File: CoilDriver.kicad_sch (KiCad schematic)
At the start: 25 parts, among them Q12 IRLML2803, Q13 SIRA99DP-T1-GE3, U3 DRV8235RTER

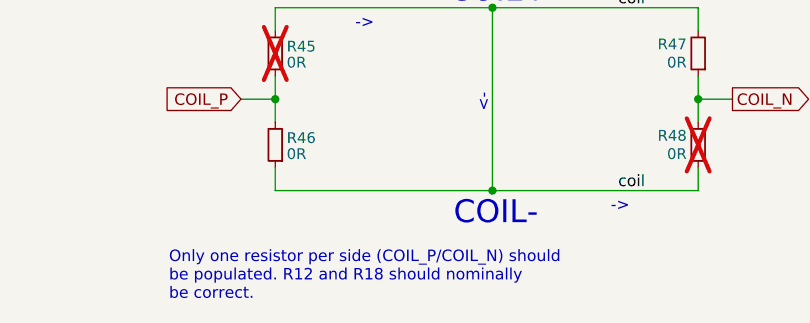
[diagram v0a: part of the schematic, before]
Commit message: Coil direction comment clarification
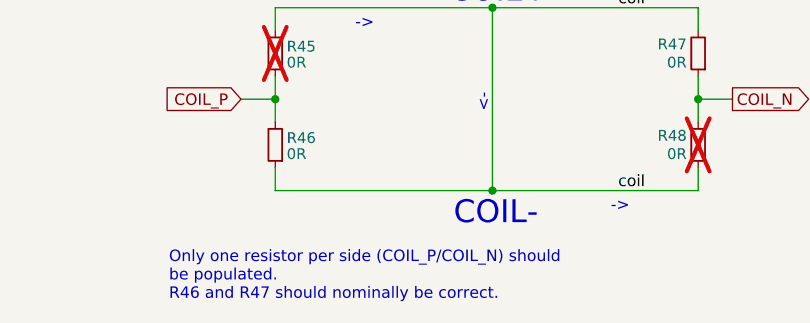
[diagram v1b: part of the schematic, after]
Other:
- note added: "Only one resistor per side (COIL_P/COIL_N) should be populated. R46 and R47 should nominally be correct."
- note removed: "Only one resistor per side (COIL_P/COIL_N) should be populated. R12 and R18 should nominally be correct."
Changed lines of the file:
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@@
 		)
 	)
-	(text "Only one resistor per side (COIL_P/COIL_N) should \nbe populated. R12 and R18 should nominally \nbe correct."
+	(text "Only one resistor per side (COIL_P/COIL_N) should \nbe populated. \nR46 and R47 should nominally be correct."
 		(exclude_from_sim no)
 		(at 42.799 168.529 0)
@@
 		)
 		(instances
-			(project "Z-"
+			(project "-Z"
 				(path "/446ceff1-46b8-4829-b15a-92d0d6c980a6/a90023fb-0fab-4c1a-9223-dcb77ef77cb2"
 					(reference "R37")
@@
 		)
 		(instances
-			(project "Z-"
+			(project "-Z"
 				(path "/446ceff1-46b8-4829-b15a-92d0d6c980a6/a90023fb-0fab-4c1a-9223-dcb77ef77cb2"
 					(reference "#PWR046")
@@
 		)
 		(instances
-			(project "Z-"
+			(project "-Z"
 				(path "/446ceff1-46b8-4829-b15a-92d0d6c980a6/a90023fb-0fab-4c1a-9223-dcb77ef77cb2"
 					(reference "R50")
@@
 		)
 		(instances
-			(project "Z-"
+			(project "-Z"
 				(path "/446ceff1-46b8-4829-b15a-92d0d6c980a6/a90023fb-0fab-4c1a-9223-dcb77ef77cb2"
 					(reference "R49")
@@
 		)
 		(instances
-			(project "Z-"
+			(project "-Z"
 				(path "/446ceff1-46b8-4829-b15a-92d0d6c980a6/a90023fb-0fab-4c1a-9223-dcb77ef77cb2"
 					(reference "R46")
@@
 		)
 		(instances
-			(project "Z-"
+			(project "-Z"
 				(path "/446ceff1-46b8-4829-b15a-92d0d6c980a6/a90023fb-0fab-4c1a-9223-dcb77ef77cb2"
 					(reference "#GND01")
@@
 		)
 		(instances
-			(project "Z-"
+			(project "-Z"
 				(path "/446ceff1-46b8-4829-b15a-92d0d6c980a6/a90023fb-0fab-4c1a-9223-dcb77ef77cb2"
 					(reference "#PWR043")
@@
 		)
 		(instances
-			(project "Z-"
+			(project "-Z"
 				(path "/446ceff1-46b8-4829-b15a-92d0d6c980a6/a90023fb-0fab-4c1a-9223-dcb77ef77cb2"
 					(reference "C9")
@@
 		)
 		(instances
-			(project "Z-"
+			(project "-Z"
 				(path "/446ceff1-46b8-4829-b15a-92d0d6c980a6/a90023fb-0fab-4c1a-9223-dcb77ef77cb2"
 					(reference "R42")
@@
 		)
 		(instances
-			(project "Z-"
+			(project "-Z"
 				(path "/446ceff1-46b8-4829-b15a-92d0d6c980a6/a90023fb-0fab-4c1a-9223-dcb77ef77cb2"
 					(reference "R43")
@@
 		)
 		(instances
-			(project "Z-"
+			(project "-Z"
 				(path "/446ceff1-46b8-4829-b15a-92d0d6c980a6/a90023fb-0fab-4c1a-9223-dcb77ef77cb2"
 					(reference "#PWR036")
@@
 		)
 		(instances
-			(project "Z-"
+			(project "-Z"
 				(path "/446ceff1-46b8-4829-b15a-92d0d6c980a6/a90023fb-0fab-4c1a-9223-dcb77ef77cb2"
 					(reference "C4")
@@
 		)
 		(instances
-			(project "Z-"
+			(project "-Z"
 				(path "/446ceff1-46b8-4829-b15a-92d0d6c980a6/a90023fb-0fab-4c1a-9223-dcb77ef77cb2"
 					(reference "R39")
@@
 		)
 		(instances
-			(project "Z-"
+			(project "-Z"
 				(path "/446ceff1-46b8-4829-b15a-92d0d6c980a6/a90023fb-0fab-4c1a-9223-dcb77ef77cb2"
 					(reference "#PWR045")
@@
 		)
 		(instances
-			(project "Z-"
+			(project "-Z"
 				(path "/446ceff1-46b8-4829-b15a-92d0d6c980a6/a90023fb-0fab-4c1a-9223-dcb77ef77cb2"
 					(reference "R51")
@@
 		)
 		(instances
-			(project "Z-"
+			(project "-Z"
 				(path "/446ceff1-46b8-4829-b15a-92d0d6c980a6/a90023fb-0fab-4c1a-9223-dcb77ef77cb2"
 					(reference "#PWR044")
@@
 		)
 		(instances
-			(project "Z-"
+			(project "-Z"
 				(path "/446ceff1-46b8-4829-b15a-92d0d6c980a6/a90023fb-0fab-4c1a-9223-dcb77ef77cb2"
 					(reference "#PWR039")
@@
 		)
 		(instances
-			(project "Z-"
+			(project "-Z"
 				(path "/446ceff1-46b8-4829-b15a-92d0d6c980a6/a90023fb-0fab-4c1a-9223-dcb77ef77cb2"
 					(reference "#PWR040")
@@
 		)
 		(instances
-			(project "Z-"
+			(project "-Z"
 				(path "/446ceff1-46b8-4829-b15a-92d0d6c980a6/a90023fb-0fab-4c1a-9223-dcb77ef77cb2"
 					(reference "Q12")
@@
 		)
 		(instances
-			(project "Z-"
+			(project "-Z"
 				(path "/446ceff1-46b8-4829-b15a-92d0d6c980a6/a90023fb-0fab-4c1a-9223-dcb77ef77cb2"
 					(reference "U3")
@@
 		)
 		(instances
-			(project "Z-"
+			(project "-Z"
 				(path "/446ceff1-46b8-4829-b15a-92d0d6c980a6/a90023fb-0fab-4c1a-9223-dcb77ef77cb2"
 					(reference "#PWR035")
@@
 		)
 		(instances
-			(project "Z-"
+			(project "-Z"
 				(path "/446ceff1-46b8-4829-b15a-92d0d6c980a6/a90023fb-0fab-4c1a-9223-dcb77ef77cb2"
 					(reference "C8")
@@
 		)
 		(instances
-			(project "Z-"
+			(project "-Z"
 				(path "/446ceff1-46b8-4829-b15a-92d0d6c980a6/a90023fb-0fab-4c1a-9223-dcb77ef77cb2"
 					(reference "#PWR038")
@@
 		)
 		(instances
-			(project "Z-"
+			(project "-Z"
 				(path "/446ceff1-46b8-4829-b15a-92d0d6c980a6/a90023fb-0fab-4c1a-9223-dcb77ef77cb2"
 					(reference "R41")
@@
 		)
 		(instances
-			(project "Z-"
+			(project "-Z"
 				(path "/446ceff1-46b8-4829-b15a-92d0d6c980a6/a90023fb-0fab-4c1a-9223-dcb77ef77cb2"
 					(reference "R47")
@@
 		)
 		(instances
-			(project "Z-"
+			(project "-Z"
 				(path "/446ceff1-46b8-4829-b15a-92d0d6c980a6/a90023fb-0fab-4c1a-9223-dcb77ef77cb2"
 					(reference "#PWR049")
@@
 		)
 		(instances
-			(project "Z-"
+			(project "-Z"
 				(path "/446ceff1-46b8-4829-b15a-92d0d6c980a6/a90023fb-0fab-4c1a-9223-dcb77ef77cb2"
 					(reference "#GND02")
@@
 		)
 		(instances
-			(project "Z-"
+			(project "-Z"
 				(path "/446ceff1-46b8-4829-b15a-92d0d6c980a6/a90023fb-0fab-4c1a-9223-dcb77ef77cb2"
 					(reference "#PWR051")
@@
 		)
 		(instances
-			(project "Z-"
+			(project "-Z"
 				(path "/446ceff1-46b8-4829-b15a-92d0d6c980a6/a90023fb-0fab-4c1a-9223-dcb77ef77cb2"
 					(reference "C5")
@@
 		)
 		(instances
-			(project "Z-"
+			(project "-Z"
 				(path "/446ceff1-46b8-4829-b15a-92d0d6c980a6/a90023fb-0fab-4c1a-9223-dcb77ef77cb2"
 					(reference "R40")
@@
 		)
 		(instances
-			(project "Z-"
+			(project "-Z"
 				(path "/446ceff1-46b8-4829-b15a-92d0d6c980a6/a90023fb-0fab-4c1a-9223-dcb77ef77cb2"
 					(reference "R45")
@@
 		)
 		(instances
-			(project "Z-"
+			(project "-Z"
 				(path "/446ceff1-46b8-4829-b15a-92d0d6c980a6/a90023fb-0fab-4c1a-9223-dcb77ef77cb2"
 					(reference "#PWR047")
@@
 		)
 		(instances
-			(project "Z-"
+			(project "-Z"
 				(path "/446ceff1-46b8-4829-b15a-92d0d6c980a6/a90023fb-0fab-4c1a-9223-dcb77ef77cb2"
 					(reference "#PWR027")
@@
 		)
 		(instances
-			(project "Z-"
+			(project "-Z"
 				(path "/446ceff1-46b8-4829-b15a-92d0d6c980a6/a90023fb-0fab-4c1a-9223-dcb77ef77cb2"
 					(reference "R38")
@@
 		)
 		(instances
-			(project "Z-"
+			(project "-Z"
 				(path "/446ceff1-46b8-4829-b15a-92d0d6c980a6/a90023fb-0fab-4c1a-9223-dcb77ef77cb2"
 					(reference "R48")
@@
 		)
 		(instances
-			(project "Z-"
+			(project "-Z"
 				(path "/446ceff1-46b8-4829-b15a-92d0d6c980a6/a90023fb-0fab-4c1a-9223-dcb77ef77cb2"
 					(reference "#PWR021")
@@
 		)
 		(instances
-			(project "Z-"
+			(project "-Z"
 				(path "/446ceff1-46b8-4829-b15a-92d0d6c980a6/a90023fb-0fab-4c1a-9223-dcb77ef77cb2"
 					(reference "D6")
@@
 		)
 		(instances
-			(project "Z-"
+			(project "-Z"
 				(path "/446ceff1-46b8-4829-b15a-92d0d6c980a6/a90023fb-0fab-4c1a-9223-dcb77ef77cb2"
 					(reference "R44")
@@
 		)
 		(instances
-			(project "Z-"
+			(project "-Z"
 				(path "/446ceff1-46b8-4829-b15a-92d0d6c980a6/a90023fb-0fab-4c1a-9223-dcb77ef77cb2"
 					(reference "F5")
@@
 		)
 		(instances
-			(project "Z-"
+			(project "-Z"
 				(path "/446ceff1-46b8-4829-b15a-92d0d6c980a6/a90023fb-0fab-4c1a-9223-dcb77ef77cb2"
 					(reference "Q13")
@@
 		)
 		(instances
-			(project "Z-"
+			(project "-Z"
 				(path "/446ceff1-46b8-4829-b15a-92d0d6c980a6/a90023fb-0fab-4c1a-9223-dcb77ef77cb2"
 					(reference "#PWR041")
@@
 		)
 		(instances
-			(project "Z-"
+			(project "-Z"
 				(path "/446ceff1-46b8-4829-b15a-92d0d6c980a6/a90023fb-0fab-4c1a-9223-dcb77ef77cb2"
 					(reference "D7")
